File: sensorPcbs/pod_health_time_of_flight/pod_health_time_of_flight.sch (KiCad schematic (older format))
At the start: 2 parts, among them J1 RJ45, U1 VL6180

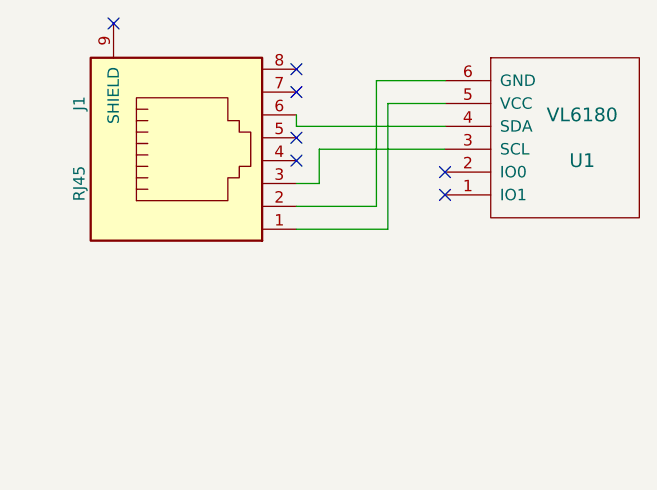
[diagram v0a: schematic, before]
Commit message: changed all the sensor PCB schematics and added the global component schematic library into each project
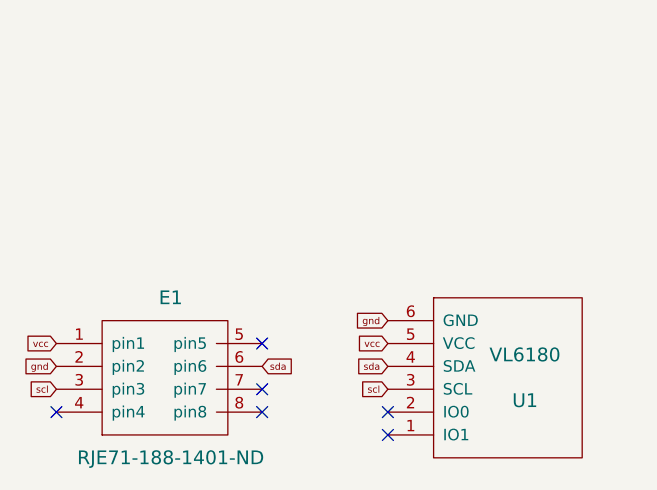
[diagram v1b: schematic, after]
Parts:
- removed J1: RJ45, Connectors:RJ45_8, symbol RJ45
- added E1: RJE71-188-1401-ND, symbol RJE71-188-1401-ND
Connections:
- net vcc: now reaches U1.5 (VCC)
- net vcc: now also E1.1 (pin1)
- net gnd: now reaches U1.6 (GND)
- net gnd: now also E1.2 (pin2)
- net scl: now reaches U1.3 (SCL)
- net scl: now also E1.3 (pin3)
- net sda: now reaches U1.4 (SDA)
- net sda: now also E1.6 (pin6)
- no-connect marks 7 -> 6
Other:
- moved on the sheet: U1
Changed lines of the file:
@@
 EESchema Schematic File Version 2
-LIBS:power
-LIBS:device
-LIBS:transistors
-LIBS:conn
-LIBS:linear
-LIBS:regul
-LIBS:74xx
-LIBS:cmos4000
-LIBS:adc-dac
-LIBS:memory
-LIBS:xilinx
-LIBS:microcontrollers
-LIBS:dsp
-LIBS:microchip
-LIBS:analog_switches
-LIBS:motorola
-LIBS:texas
-LIBS:intel
-LIBS:audio
-LIBS:interface
-LIBS:digital-audio
-LIBS:philips
-LIBS:display
-LIBS:cypress
-LIBS:siliconi
-LIBS:opto
-LIBS:atmel
-LIBS:contrib
-LIBS:valves
 LIBS:vl6180
+LIBS:customSchematics
 LIBS:pod_health_time_of_flight-cache
 EELAYER 25 0
@@
 $EndDescr
 $Comp
-L RJ45 J1
-U 1 1 58D9D58C
-P 2300 1700
-F 0 "J1" H 2500 2200 50  0000 C CNN
-F 1 "RJ45" H 2150 2200 50  0000 C CNN
-F 2 "Connectors:RJ45_8" H 2300 1700 50  0001 C CNN
-F 3 "" H 2300 1700 50  0001 C CNN
-	1    2300 1700
-	0    -1   -1   0
-$EndComp
-NoConn ~ 2750 1350
-NoConn ~ 2750 1450
-NoConn ~ 1950 1150
-NoConn ~ 2750 1650
-NoConn ~ 2750 1750
-$Comp
 L VL6180 U1
 U 1 1 58DA9061
-P 3600 1650
-F 0 "U1" H 4000 1550 60  0000 C CNN
-F 1 "VL6180" H 4000 1750 60  0000 C CNN
-F 2 "vl1680_footprint:VL6180" H 3600 1650 60  0001 C CNN
-F 3 "" H 3600 1650 60  0001 C CNN
-	1    3600 1650
+P 3350 2700
+F 0 "U1" H 3750 2600 60  0000 C CNN
+F 1 "VL6180" H 3750 2800 60  0000 C CNN
+F 2 "vl1680_footprint:VL6180" H 3350 2700 60  0001 C CNN
+F 3 "" H 3350 2700 60  0001 C CNN
+	1    3350 2700
 	1    0    0    -1
 $EndComp
-Wire Wire Line
-	3400 1500 3150 1500
-Wire Wire Line
-	3150 1500 3150 2050
-Wire Wire Line
-	3150 2050 2750 2050
-Wire Wire Line
-	3400 1400 3100 1400
-Wire Wire Line
-	3100 1400 3100 1950
-Wire Wire Line
-	3100 1950 2750 1950
-Wire Wire Line
-	3400 1700 2850 1700
-Wire Wire Line
-	2850 1700 2850 1850
-Wire Wire Line
-	2850 1850 2750 1850
-Wire Wire Line
-	3400 1600 2750 1600
-Wire Wire Line
-	2750 1600 2750 1550
-NoConn ~ 3400 1800
-NoConn ~ 3400 1900
+NoConn ~ 3150 2850
+NoConn ~ 3150 2950
+$Comp
+L RJE71-188-1401-ND E1
+U 1 1 597120E6
+P 1900 2550
+F 0 "E1" H 2200 2750 60  0000 C CNN
+F 1 "RJE71-188-1401-ND" H 2200 2050 60  0000 C CNN
+F 2 "" H 1900 2550 60  0001 C CNN
+F 3 "" H 1900 2550 60  0001 C CNN
+	1    1900 2550
+	1    0    0    -1
+$EndComp
+Text GLabel 1700 2550 0    30   Input ~ 0
+vcc
+Text GLabel 1700 2650 0    30   Input ~ 0
+gnd
+Text GLabel 1700 2750 0    30   Input ~ 0
+scl
+Text GLabel 2600 2650 2    30   Input ~ 0
+sda
+Text GLabel 3150 2550 0    30   Input ~ 0
+vcc
+Text GLabel 3150 2450 0    30   Input ~ 0
+gnd
+Text GLabel 3150 2750 0    30   Input ~ 0
+scl
+Text GLabel 3150 2650 0    30   Input ~ 0
+sda
+NoConn ~ 2600 2550
+NoConn ~ 2600 2750
+NoConn ~ 2600 2850
+NoConn ~ 1700 2850
 $EndSCHEMATC

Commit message: added all the ferkin new ethernet shields to the sensor pcbs
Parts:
- E1: footprint (none) -> footprints:RJE71-188-1401-ND
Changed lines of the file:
@@
 F 0 "E1" H 2200 2750 60  0000 C CNN
 F 1 "RJE71-188-1401-ND" H 2200 2050 60  0000 C CNN
-F 2 "" H 1900 2550 60  0001 C CNN
+F 2 "footprints:RJE71-188-1401-ND" H 1900 2550 60  0001 C CNN
 F 3 "" H 1900 2550 60  0001 C CNN
 	1    1900 2550

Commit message: fixed the tof according to viks wants
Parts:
- U1: footprint vl1680_footprint:VL6180 -> vl1680_footprint:tof
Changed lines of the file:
@@
 EESchema Schematic File Version 2
+LIBS:power
+LIBS:device
+LIBS:transistors
+LIBS:conn
+LIBS:linear
+LIBS:regul
+LIBS:74xx
+LIBS:cmos4000
+LIBS:adc-dac
+LIBS:memory
+LIBS:xilinx
+LIBS:microcontrollers
+LIBS:dsp
+LIBS:microchip
+LIBS:analog_switches
+LIBS:motorola
+LIBS:texas
+LIBS:intel
+LIBS:audio
+LIBS:interface
+LIBS:digital-audio
+LIBS:philips
+LIBS:display
+LIBS:cypress
+LIBS:siliconi
+LIBS:opto
+LIBS:atmel
+LIBS:contrib
+LIBS:valves
 LIBS:vl6180
 LIBS:customSchematics
@@
 F 0 "U1" H 3750 2600 60  0000 C CNN
 F 1 "VL6180" H 3750 2800 60  0000 C CNN
-F 2 "vl1680_footprint:VL6180" H 3350 2700 60  0001 C CNN
+F 2 "vl1680_footprint:tof" H 3350 2700 60  0001 C CNN
 F 3 "" H 3350 2700 60  0001 C CNN
 	1    3350 2700
